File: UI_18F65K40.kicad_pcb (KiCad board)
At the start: 2 copper layers, 115 x 70 mm, 153 parts, among them J101 MOLEX_KK-254, J102 IDC 2x15, J103 IDC 2x3, J301 Pin_Header_01x06, J302 GS2, J303 GS2, Q201 BSS84, Q202 BSS138, Q301 BSS84, Q302 BSS138, SW201 EC11K1524402, SW202 EC11K1524402, SW203 B3W-9000-RG2N, SW204 B3W-9000-RG2N, SW205 B3W-9000-RG2N, SW206 B3W-9000-RG2N, U201 74LVC1G125, U301 MCP6V81U, U302 MCP79410, U303 74LVC2G14, U304 74LVC1G126, U305 74HC08, U306 74LVC1G125, U307 PIC18F65K40-I/PT, U308 24LC512, U309 24LC512, Y301 32.768kHz, Y302 16MHz

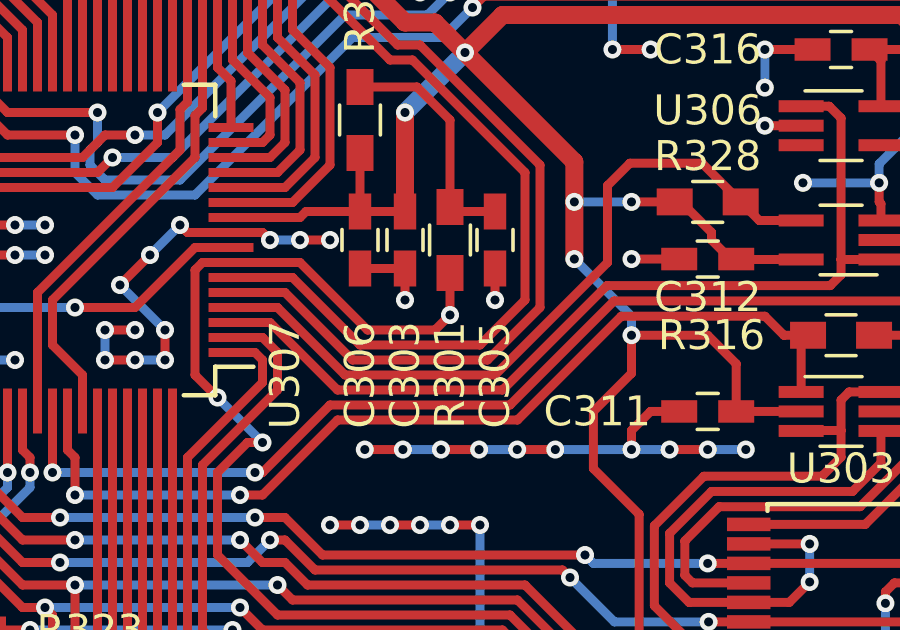
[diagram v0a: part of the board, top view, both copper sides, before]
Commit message: Removed useless via from the VPP net near R301
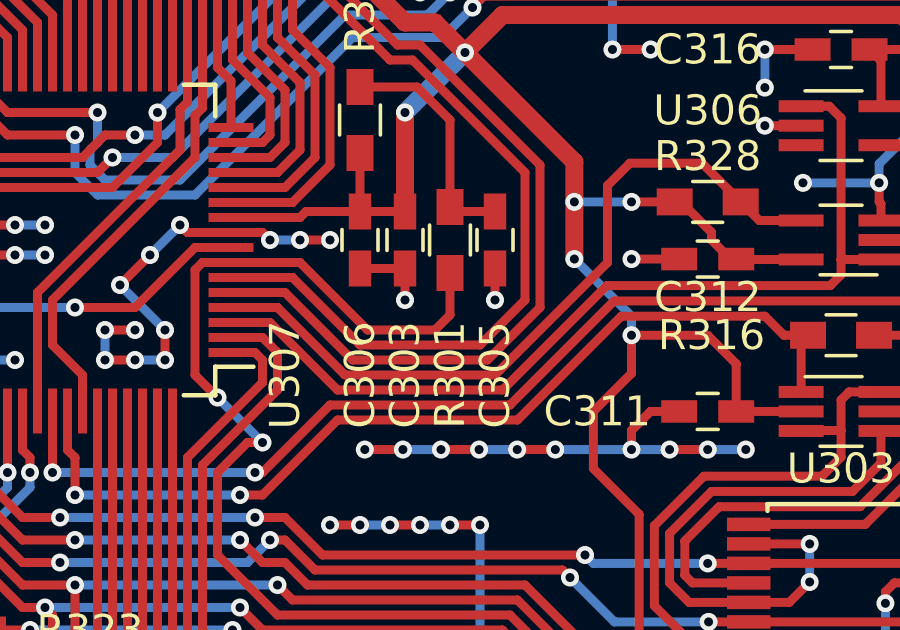
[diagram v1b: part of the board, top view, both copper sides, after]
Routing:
- net /Microcontroller & Peripherals/VPP: vias 3 -> 2
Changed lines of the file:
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@@
     (thickness 1.6)
     (drawings 14)
-    (tracks 1850)
+    (tracks 1849)
     (zones 0)
     (modules 153)
@@
   (segment (start 167.5 98) (end 168 97.5) (width 0.3) (layer F.Cu) (net 31))
   (segment (start 168 96.1) (end 168 97.5) (width 0.3) (layer F.Cu) (net 31))
-  (via (at 168 97.5) (size 0.6) (drill 0.3) (layers F.Cu B.Cu) (net 31))
   (segment (start 163 95.75) (end 165.25 98) (width 0.3) (layer F.Cu) (net 31))
   (segment (start 163 95.75) (end 160.7 95.75) (width 0.3) (layer F.Cu) (net 31))

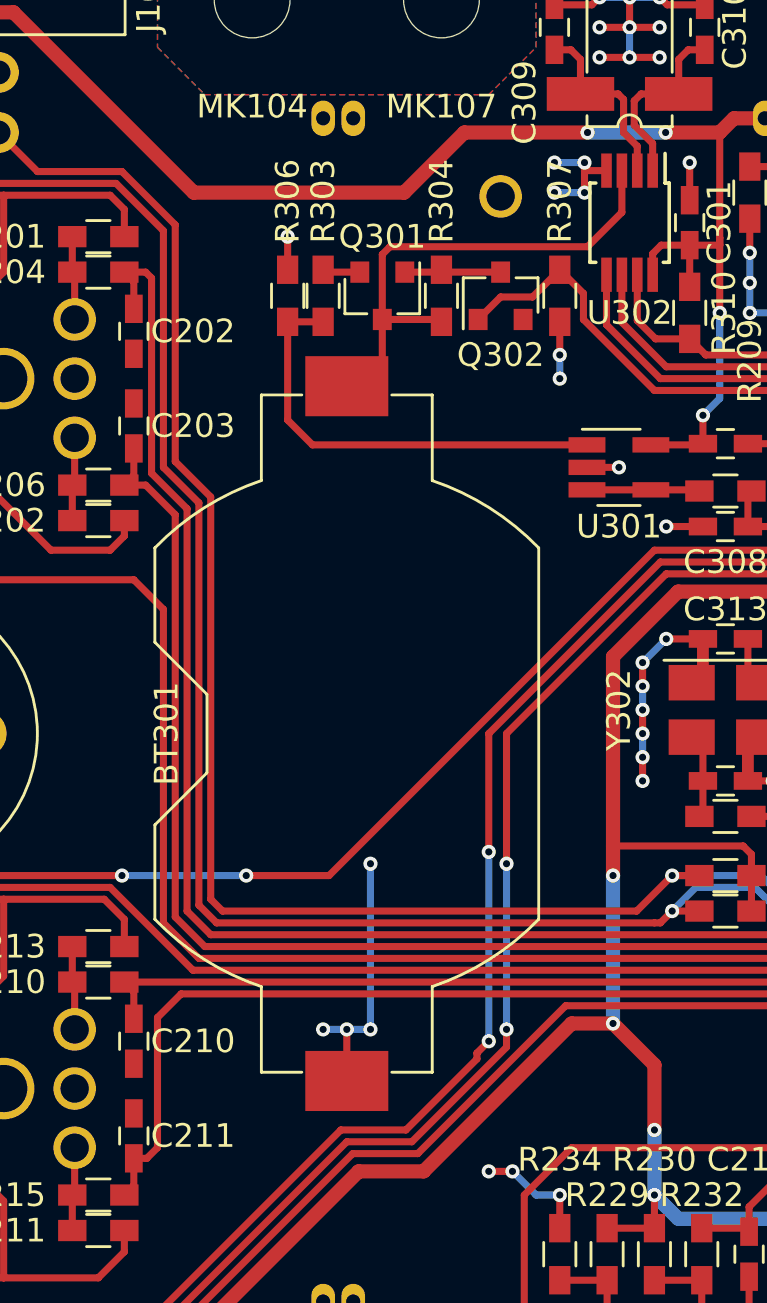
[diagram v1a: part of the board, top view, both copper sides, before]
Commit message: Flipped Q301 since it was backwards, updated netlist, PCB layout, PDF schematic
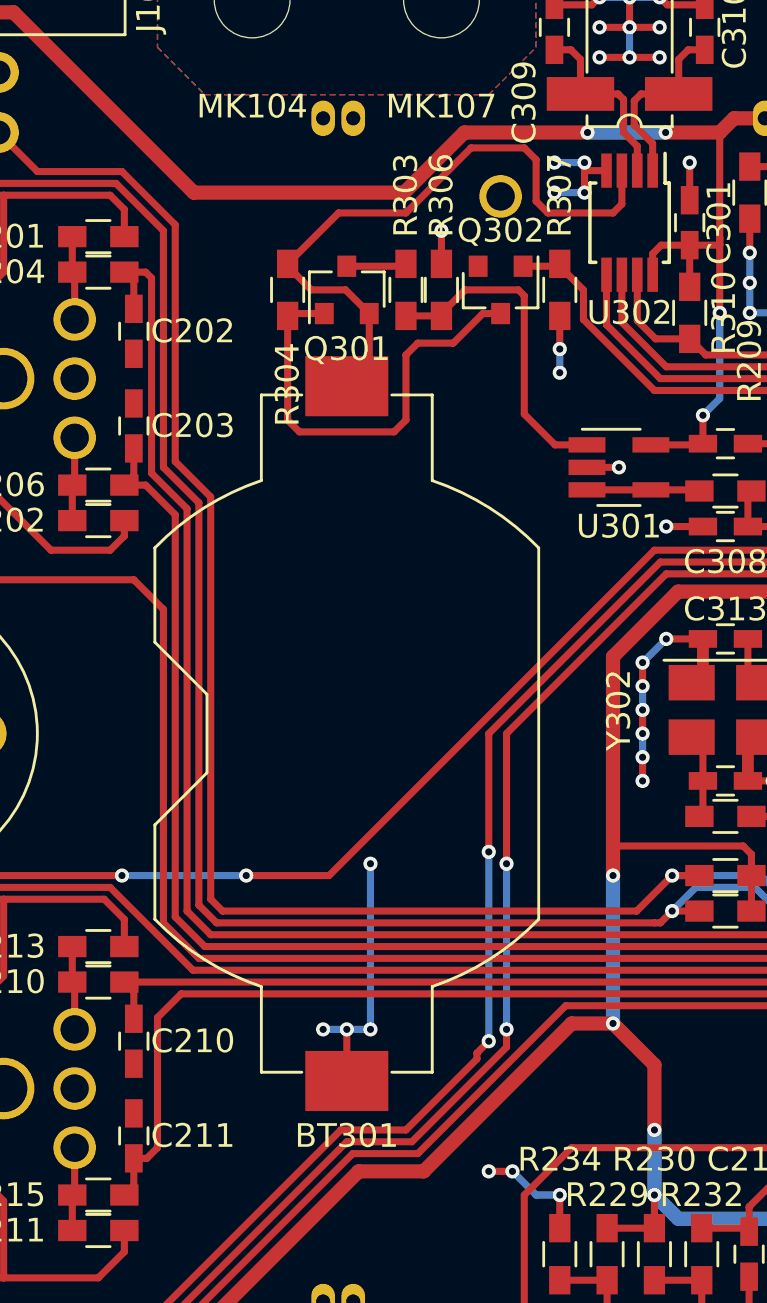
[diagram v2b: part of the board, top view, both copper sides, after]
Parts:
- moved R304 6.50 mm to (121.5, 76.2), turned to 270 degrees
- moved R306 6.50 mm to (128.0, 76.2)
- moved R303 3.51 mm to (126.5, 76.2)
- moved Q301 1.52 mm to (124.0, 76.2), turned to 90 degrees
- moved Q302 0.25 mm to (130.5, 76.2), turned to 270 degrees
- moved R307 0.25 mm to (133.0, 76.2)
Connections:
- Q301 pad 2: Net-(Q301-Pad2) -> Net-(BT301-Pad1)
- Q301 pad 3: Net-(BT301-Pad1) -> Net-(Q301-Pad3)
- R303 pad 1: Net-(Q301-Pad2) -> Net-(Q301-Pad3)
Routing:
- net Net-(Q301-Pad1): track 4.13 -> 18.9 mm
- net Net-(BT301-Pad1): track 21.8 -> 27.8 mm
- net Net-(R303-Pad2): track 18.7 -> 13.8 mm
- net Net-(Q301-Pad3): track 0.00 -> 2.54 mm
- net /Microcontroller & Peripherals/EN_VBAT: track 34.3 -> 31.8 mm
- net Net-(Q301-Pad2): track 1.59 -> 0.00 mm
